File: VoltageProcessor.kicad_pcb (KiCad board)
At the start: 2 copper layers, 25.4 x 100 mm, 29 parts, among them J1 PJ301M-12, J2 PJ301M-12, J3 PJ301M-12, J5 Eurorack power, J7 PJ301M-12, U1 TL074

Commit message: IO Placement
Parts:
- removed the J3 at (101.2, 149.8)
- removed R15: 100k, Resistor_THT:R_Axial_DIN0204_L3.6mm_D1.6mm_P7.62mm_Horizontal
- added J4: PJ301M-12, Eurocad:PJ301M-12, F.Cu at (114.3, 149.8)
- added R13: 1k, Resistor_THT:R_Axial_DIN0204_L3.6mm_D1.6mm_P7.62mm_Horizontal, F.Cu at (127.9, 40.9)
- C1, C2: value 47uF -> 0.1uF
- C5, C6: value 0.1uF -> 47uF
- R12, R9: value 1k -> 100k
- R14: value 100k -> 1k
- moved J5 87.1 mm to (100.7, 149.8), turned to 180 degrees
- moved J2 86.0 mm to (114.3, 63.8), turned to 0 degrees
- moved J3 8.63 mm to (106.3, 139.3), turned to 0 degrees
- moved U1 1.29 mm to (99.9, 117.5)
- moved J1 0.56 mm to (100.7, 63.8)
- renumbered J5 to J3, J7 to J5, RV3 to RV1, RV1 to RV3
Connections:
- J2 pad 2: Net-(J2-Pad2) -> unconnected-(J2-Pad2)
- J2 pad 3: unconnected-(J2-Pad3) -> Net-(J2-Pad3)
- J5 pad 2: unconnected-(J7-Pad2) -> Net-(J5-Pad2)
- J5 pad 3: Net-(J7-Pad3) -> unconnected-(J5-Pad3)
- R1 pad 1: unconnected-(R1-Pad1) -> Net-(R1-Pad1)
- R10 pad 1: GND -> Net-(U1C--)
- R10 pad 2: Net-(U1D--) -> Net-(R10-Pad2)
- R11 pad 1: Net-(R11-Pad1) -> GND
- R12 pad 1: Net-(R12-Pad1) -> Net-(U1D-+)
- R12 pad 2: Net-(J3-Pad2) -> Net-(R12-Pad2)
- R14 pad 1: Net-(R14-Pad1) -> Net-(R12-Pad2)
- R14 pad 2: Net-(U1D-+) -> Net-(J5-Pad2)
- R2 pad 1: Net-(U1A--) -> Net-(R2-Pad1)
- R2 pad 2: Net-(R14-Pad1) -> Net-(U1B-+)
- R3 pad 1: Net-(R14-Pad1) -> Net-(U1A--)
- R3 pad 2: Net-(U1C--) -> Net-(R3-Pad2)
- R4 pad 1: unconnected-(R4-Pad1) -> Net-(U1B-+)
- R4 pad 2: Net-(U1B-+) -> Net-(R4-Pad2)
- R5 pad 1: Net-(U1B-+) -> Net-(R3-Pad2)
- R5 pad 2: Net-(R11-Pad1) -> Net-(U1C--)
- R6 pad 1: Net-(R11-Pad1) -> Net-(R4-Pad2)
- R8 pad 1: Net-(U1C--) -> Net-(R3-Pad2)
- R8 pad 2: Net-(R8-Pad2) -> Net-(U1D-+)
- R9 pad 1: Net-(R8-Pad2) -> Net-(R4-Pad2)
- R9 pad 2: Net-(J2-Pad2) -> Net-(U1D--)
- RV1 pad 1: +12V -> Net-(J1-Pad3)
- RV1 pad 2: Net-(R7-Pad1) -> Net-(R1-Pad1)
- RV1 pad 3: -12V -> GND
- RV2 pad 1: Net-(J7-Pad3) -> Net-(J2-Pad3)
- RV2 pad 2: unconnected-(RV2-Pad2) -> Net-(R2-Pad1)
- RV3 pad 1: Net-(J1-Pad3) -> +12V
- RV3 pad 2: unconnected-(RV1-Pad2) -> Net-(R7-Pad1)
- RV3 pad 3: GND -> -12V
- U1 pad 1: Net-(R14-Pad1) -> Net-(R3-Pad2)
- U1 pad 14: Net-(R12-Pad1) -> Net-(R12-Pad2)
- U1 pad 7: Net-(R11-Pad1) -> Net-(R4-Pad2)
- U1 pad 8: Net-(R8-Pad2) -> Net-(R10-Pad2)

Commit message: Pre route
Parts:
- C1, C2: footprint Capacitor_THT:C_Radial_D5.0mm_H11.0mm_P2.00mm -> Capacitor_THT:C_Disc_D5.0mm_W2.5mm_P2.50mm; moved to B.Cu
- C5, C6: footprint Capacitor_THT:C_Disc_D5.0mm_W2.5mm_P2.50mm -> Capacitor_THT:C_Radial_D5.0mm_H11.0mm_P2.00mm; moved to B.Cu
- moved R13 82.2 mm to (96.7, 116.9), turned to -90 degrees
- moved C2 67.9 mm to (101.9, 137.1), turned to 90 degrees
- moved C1 66.5 mm to (101.9, 128.3), turned to -90 degrees
- moved C6 48.0 mm to (106.9, 134.6), turned to -90 degrees
- moved C5 47.4 mm to (106.9, 128.2), turned to -90 degrees
- moved R1 45.9 mm to (99.5, 89.5), turned to -90 degrees
- moved R5 44.9 mm to (96.7, 103.5)
- moved R7 44.8 mm to (101.9, 124.5), turned to 90 degrees
- moved R3 44.3 mm to (96.7, 89.5), turned to -90 degrees
- moved R8 44.3 mm to (96.7, 106.3), turned to -90 degrees
- moved R10 43.5 mm to (99.3, 124.5), turned to 90 degrees
- moved R14 41.4 mm to (107.7, 146.3), turned to -90 degrees
- moved R12 37.0 mm to (104.5, 124.6), turned to 90 degrees
- moved C4 34.7 mm to (118.5, 117.8), turned to 90 degrees
- moved C3 34.3 mm to (118.5, 109.5), turned to -90 degrees
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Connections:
- R1 pad 2: Net-(U1A--) -> Net-(U1B-+)
- R2 pad 2: Net-(U1B-+) -> Net-(U1A--)
- R3 pad 1: Net-(U1A--) -> Net-(U1B-+)
- R4 pad 1: Net-(U1B-+) -> Net-(U1A--)
- U1 pad 1: Net-(R3-Pad2) -> Net-(R4-Pad2)
- U1 pad 6: GND -> unconnected-(U1B---Pad6)
- U1 pad 7: Net-(R4-Pad2) -> Net-(R3-Pad2)
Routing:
- net Net-(J2-Pad3): track 0.00 -> 28.7 mm
- net Net-(J1-Pad3): track 0.00 -> 28.2 mm
- net Net-(U1C--): track 0.00 -> 27.4 mm
- net Net-(R3-Pad2): track 0.00 -> 12.4 mm
- net +12V: track 0.00 -> 10.2 mm
- net Net-(R4-Pad2): track 0.00 -> 8.81 mm, vias 0 -> 1
- net Net-(U1B-+): track 0.00 -> 8.79 mm
- net Net-(R10-Pad2): track 0.00 -> 5.39 mm
- net Net-(R2-Pad1): track 0.00 -> 4.25 mm
- net Net-(R1-Pad1): track 0.00 -> 4.00 mm
- net -12V: track 0.00 -> 2.54 mm

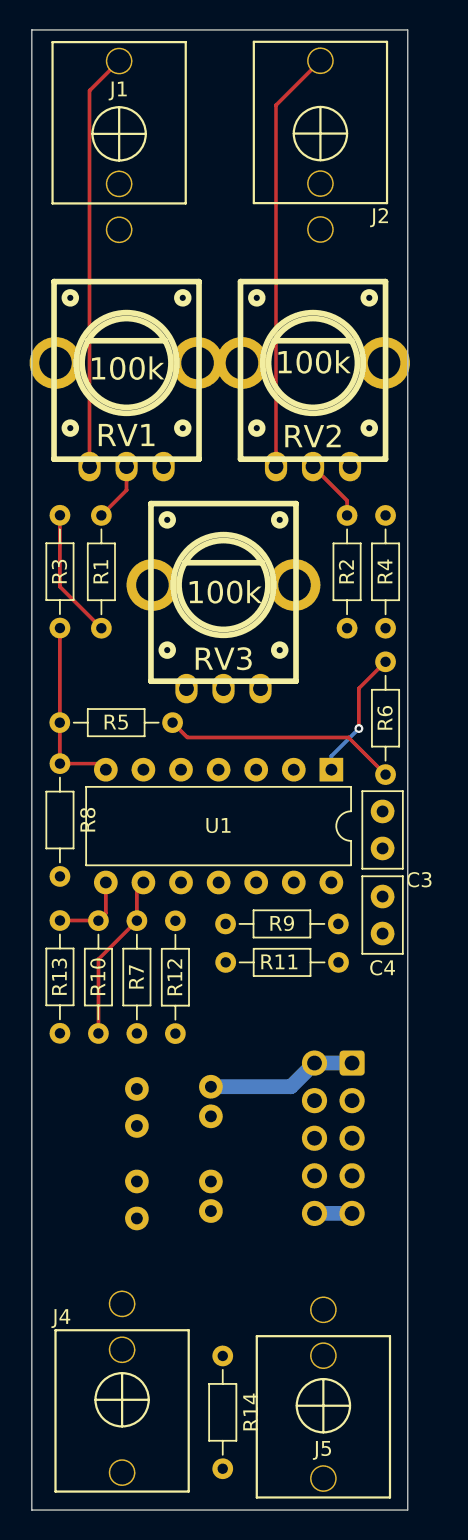
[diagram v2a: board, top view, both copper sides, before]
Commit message: Done with routing but DRC issues
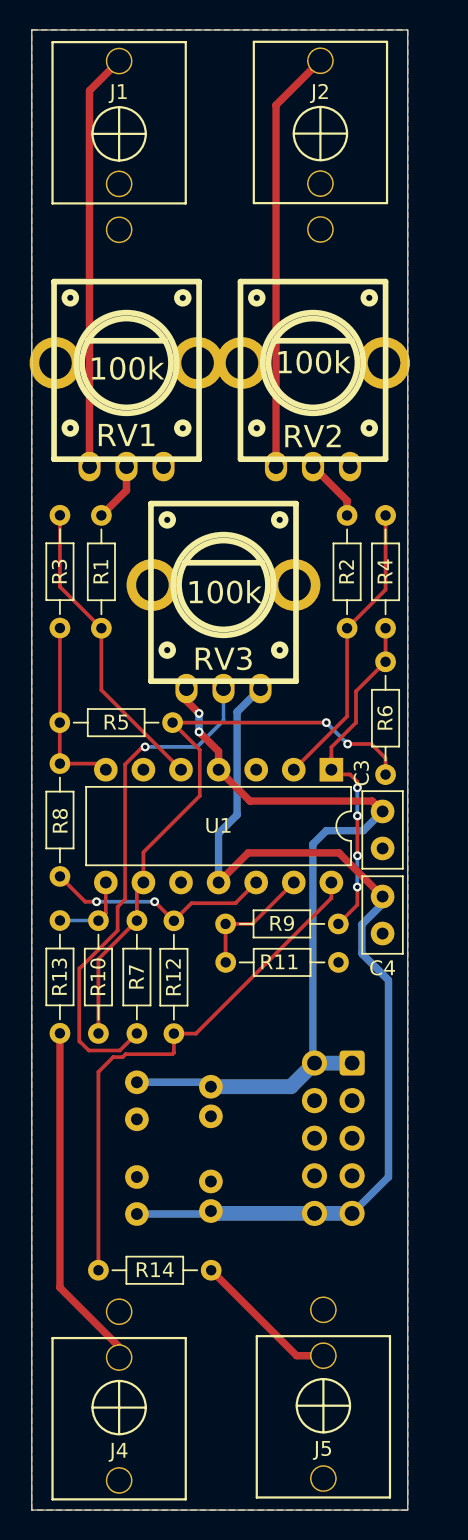
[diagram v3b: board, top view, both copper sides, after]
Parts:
- moved R14 10.2 mm to (99.3, 140.6), turned to 0 degrees
- moved R12 7.62 mm to (104.4, 116.9), turned to -90 degrees
- moved C2 2.80 mm to (101.9, 134.2), turned to -90 degrees
- moved J4 0.56 mm to (100.7, 149.8)
- moved C1 0.45 mm to (101.9, 127.8)
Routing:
- net -12V: track 2.54 -> 65.8 mm
- net +12V: track 10.2 -> 54.4 mm, vias 0 -> 2
- net Net-(R12-Pad2): track 0.00 -> 35.8 mm
- net Net-(R7-Pad1): track 0.00 -> 34.6 mm, vias 0 -> 1
- net Net-(J4-Pad2): track 0.00 -> 23.1 mm
- net Net-(U1A--): track 0.00 -> 19.7 mm
- net Net-(U1D-+): track 0.00 -> 15.6 mm, vias 0 -> 2
- net Net-(R4-Pad2): track 8.81 -> 24.2 mm, vias 1 -> 4
- net Net-(U1C--): track 27.4 -> 41.2 mm, vias 0 -> 2
- net Net-(U1B-+): track 8.79 -> 20.6 mm
- net Net-(J5-Pad2): track 0.00 -> 9.97 mm
- net Net-(U1D--): track 0.00 -> 8.37 mm
- added copper zone on B.Cu, net GND
- added copper zone on F.Cu, net GND

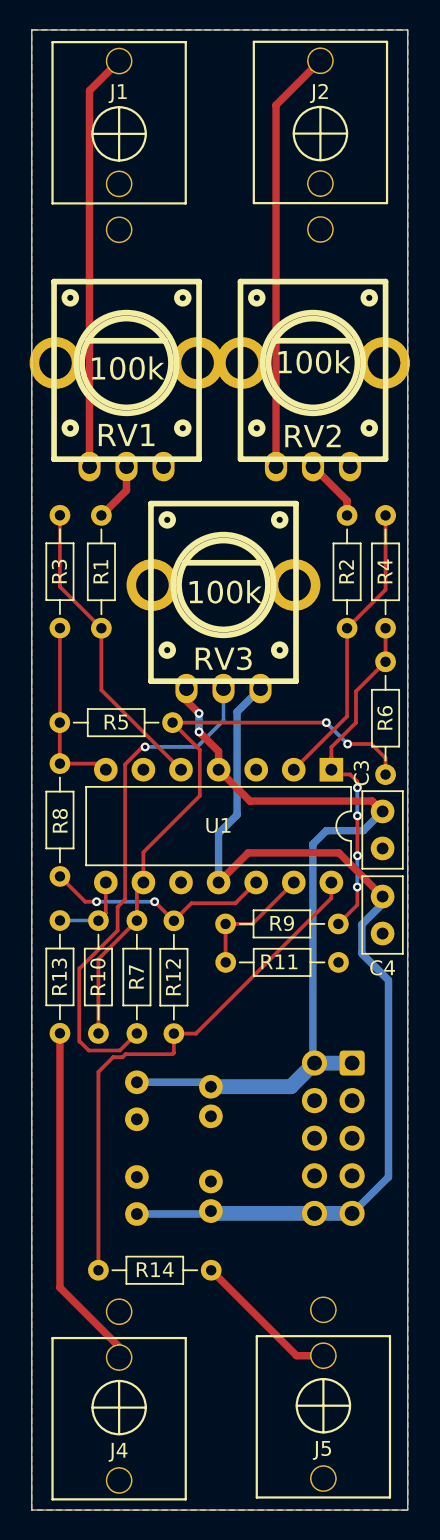
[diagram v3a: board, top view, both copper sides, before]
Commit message: Fix most DRC errors
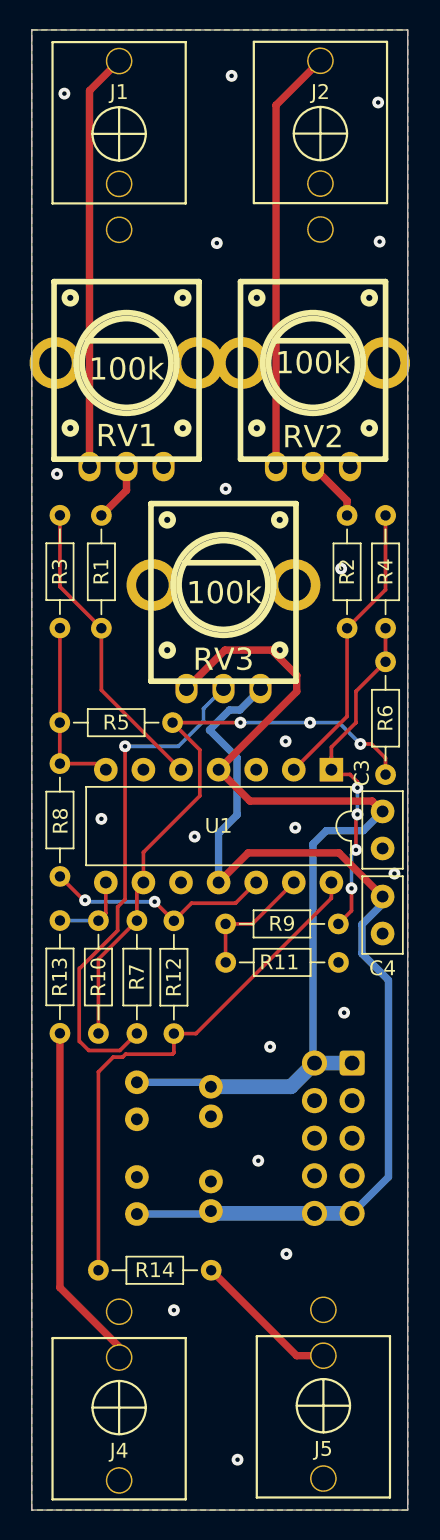
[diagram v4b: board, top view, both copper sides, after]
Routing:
- net +12V: track 54.4 -> 66.7 mm, vias 2 -> 0
- net -12V: track 65.8 -> 67.8 mm
- net Net-(U1C--): vias 2 -> 3
- net GND: vias 0 -> 19

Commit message: Add silkscreen text, and last DRC issues
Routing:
- net GND: track 0.00 -> 17.9 mm, vias 19 -> 21
- net Net-(U1C--): vias 3 -> 2
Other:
- board text added: "Voltage Processor"
- board text added: "joppeboeve.nl"
- board text added: "rev 0.1"
